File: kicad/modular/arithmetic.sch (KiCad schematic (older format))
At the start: 31 parts, among them J4 Header, J5 DIFFX, J6 DIFFY, J7 SUM, U5 OPA197, U6 OPA2197

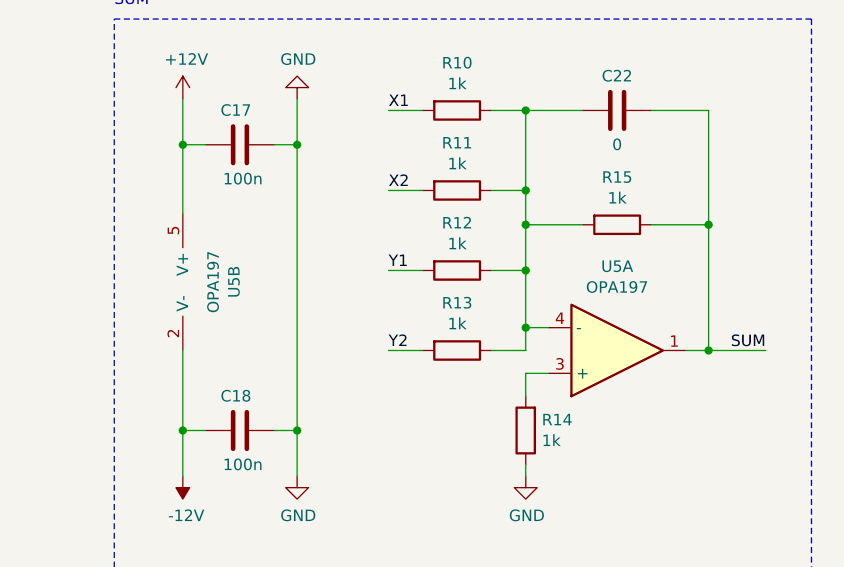
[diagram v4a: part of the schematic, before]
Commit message: fixed generic opamp symbol pin layout, updated pcb of arithmetic board
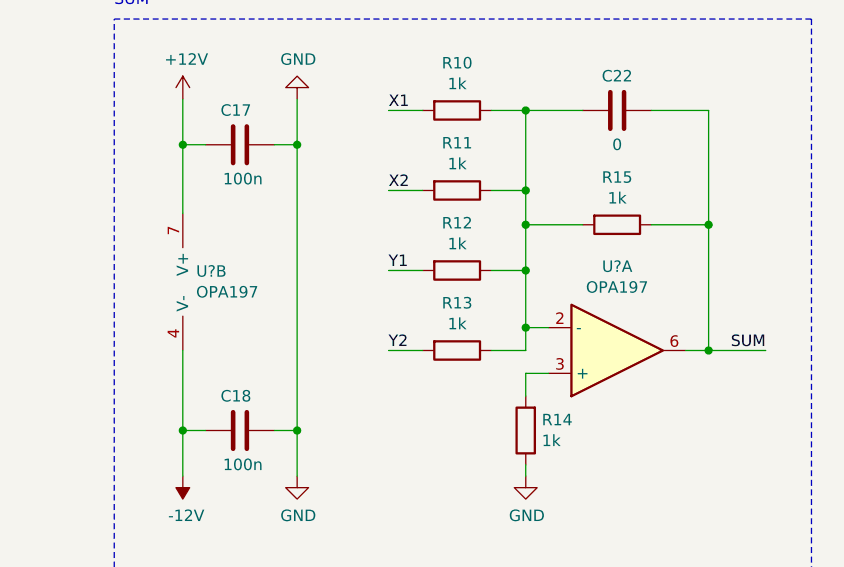
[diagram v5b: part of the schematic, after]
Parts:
- removed U5: OPA197, Package_SO:SOIC-8_3.9x4.9mm_P1.27mm, symbol Device:Opamp_Generic
- added U? (x2): OPA197, symbol Device:Opamp_Generic_SOIC8
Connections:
- net +12V: now also U?.7 (V+)
- net -12V: now also U?.4 (V-)
- net SUM: now also U?.6
- net at R14.2: now also U?.3 (+)
- net at C22.2, R10.1, R11.1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: now also U?.2 (-)
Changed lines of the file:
@@
-$EndComp
-$Comp
-L Device:Opamp_Generic U5
-U 1 1 5D52810C
-P 3900 6200
-F 0 "U5" H 3900 5833 50  0000 C CNN
-F 1 "OPA197" H 3900 5924 50  0000 C CNN
-F 2 "Package_SO:SOIC-8_3.9x4.9mm_P1.27mm" H 3850 6200 50  0001 C CNN
-F 3 "~" H 3850 6200 50  0001 C CNN
-	1    3900 6200
-	1    0    0    1
 $EndComp
 $Comp
@@
 	1    2000 5100
 	1    0    0    -1
-$EndComp
-$Comp
-L Device:Opamp_Generic U5
-U 2 1 5D52C13C
-P 1800 5900
-F 0 "U5" V 1375 5900 50  0000 C CNN
-F 1 "OPA197" V 1466 5900 50  0000 C CNN
-F 2 "Package_SO:SOIC-8_3.9x4.9mm_P1.27mm" H 1750 5900 50  0001 C CNN
-F 3 "~" H 1750 5900 50  0001 C CNN
-	2    1800 5900
-	-1   0    0    -1
 $EndComp
 Wire Notes Line
@@
 Wire Wire Line
 	6600 5050 6850 5050
+$Comp
+L Device:Opamp_Generic_SOIC8 U?
+U 1 1 5D8E1171
+P 3900 6200
+F 0 "U?" H 3900 5833 50  0000 C CNN
+F 1 "OPA197" H 3900 5924 50  0000 C CNN
+F 2 "" H 3850 6200 50  0001 C CNN
+F 3 "~" H 3850 6200 50  0001 C CNN
+	1    3900 6200
+	1    0    0    1
+$EndComp
+$Comp
+L Device:Opamp_Generic_SOIC8 U?
+U 2 1 5D8E2386
+P 2200 5900
+F 0 "U?" H 2058 5946 50  0000 L CNN
+F 1 "OPA197" H 2058 5855 50  0000 L CNN
+F 2 "" H 2150 5900 50  0001 C CNN
+F 3 "~" H 2150 5900 50  0001 C CNN
+	2    2200 5900
+	1    0    0    -1
+$EndComp
 $EndSCHEMATC

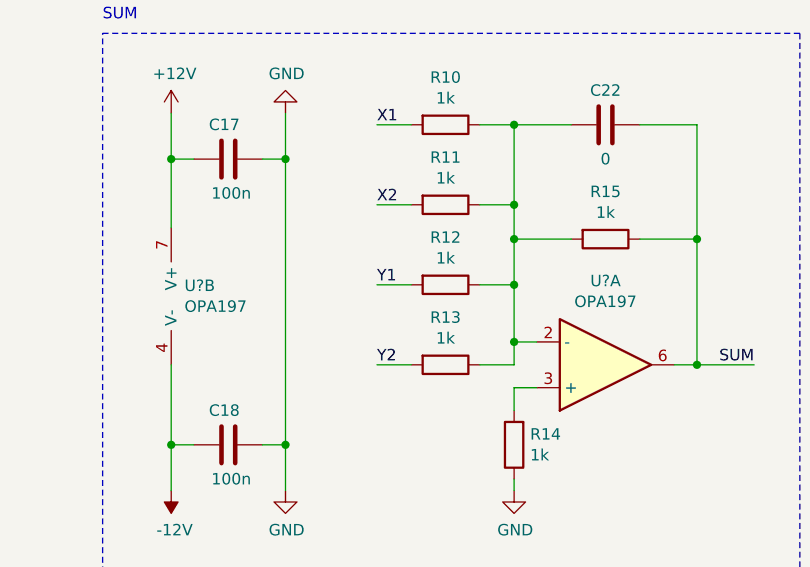
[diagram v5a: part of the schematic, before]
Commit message: added test points to experimental adc and buffer boards, improved schematic, assigned footprints
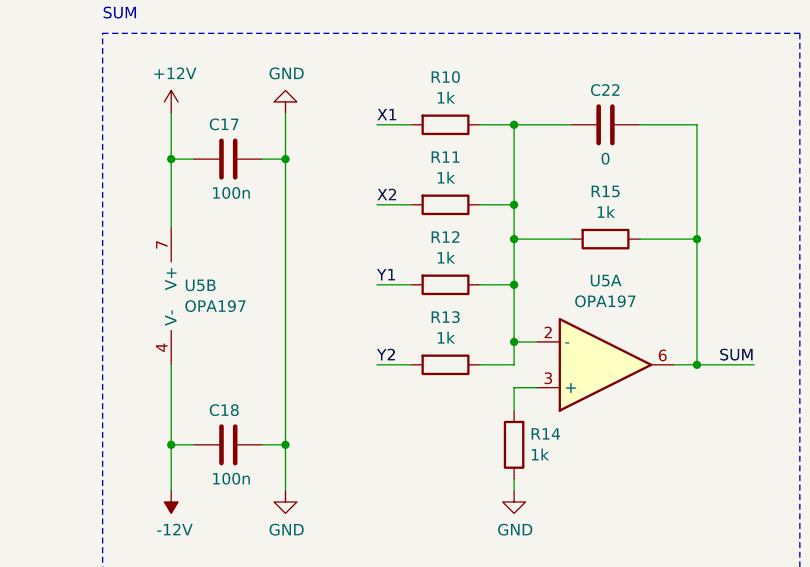
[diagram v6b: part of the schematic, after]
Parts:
- U5: renamed from U?; footprint (none) -> Package_SO:SOIC-8_3.9x4.9mm_P1.27mm
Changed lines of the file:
@@
 	6600 5050 6850 5050
 $Comp
-L Device:Opamp_Generic_SOIC8 U?
+L Device:Opamp_Generic_SOIC8 U5
 U 1 1 5D8E1171
 P 3900 6200
-F 0 "U?" H 3900 5833 50  0000 C CNN
+F 0 "U5" H 3900 5833 50  0000 C CNN
 F 1 "OPA197" H 3900 5924 50  0000 C CNN
-F 2 "" H 3850 6200 50  0001 C CNN
+F 2 "Package_SO:SOIC-8_3.9x4.9mm_P1.27mm" H 3850 6200 50  0001 C CNN
 F 3 "~" H 3850 6200 50  0001 C CNN
 	1    3900 6200
@@
 $EndComp
 $Comp
-L Device:Opamp_Generic_SOIC8 U?
+L Device:Opamp_Generic_SOIC8 U5
 U 2 1 5D8E2386
 P 2200 5900
-F 0 "U?" H 2058 5946 50  0000 L CNN
+F 0 "U5" H 2058 5946 50  0000 L CNN
 F 1 "OPA197" H 2058 5855 50  0000 L CNN
-F 2 "" H 2150 5900 50  0001 C CNN
+F 2 "Package_SO:SOIC-8_3.9x4.9mm_P1.27mm" H 2150 5900 50  0001 C CNN
 F 3 "~" H 2150 5900 50  0001 C CNN
 	2    2200 5900
